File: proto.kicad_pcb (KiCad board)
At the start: 2 copper layers, 100 x 100 mm, 159 parts

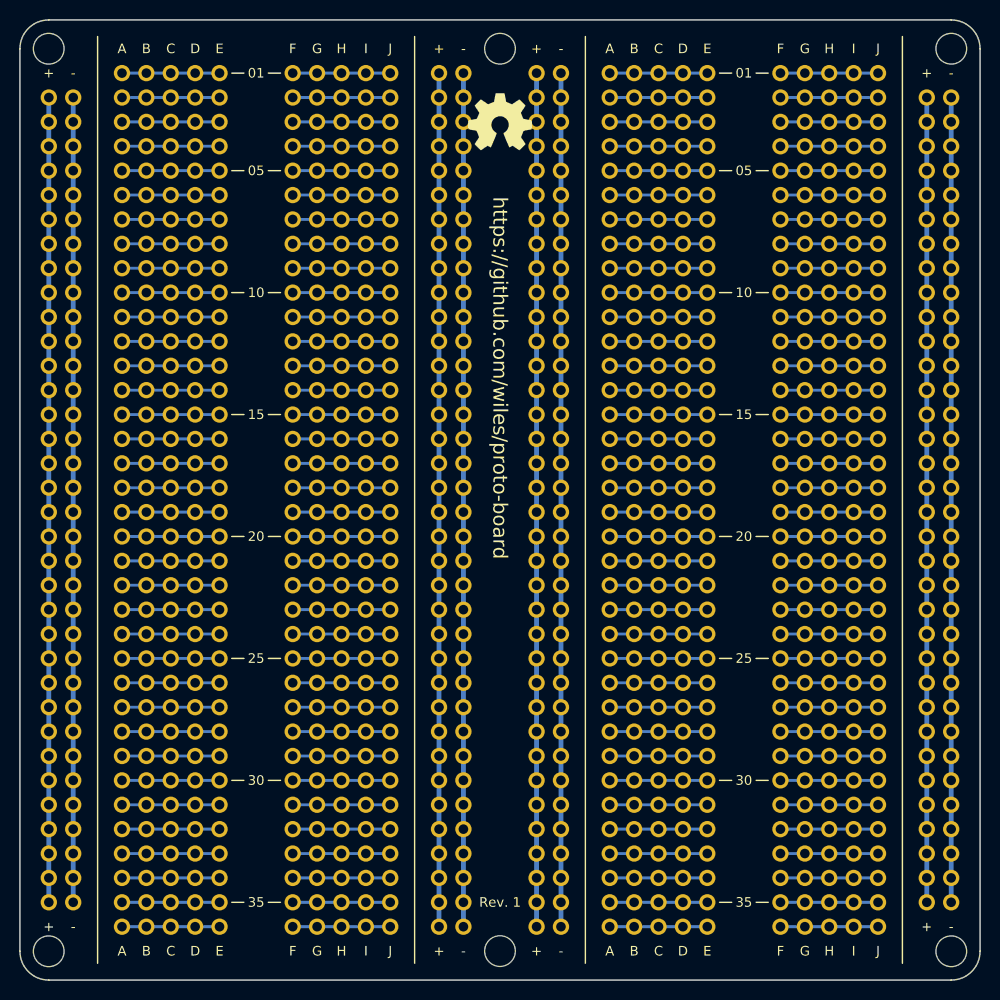
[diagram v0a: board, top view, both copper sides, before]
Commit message: increased trace width
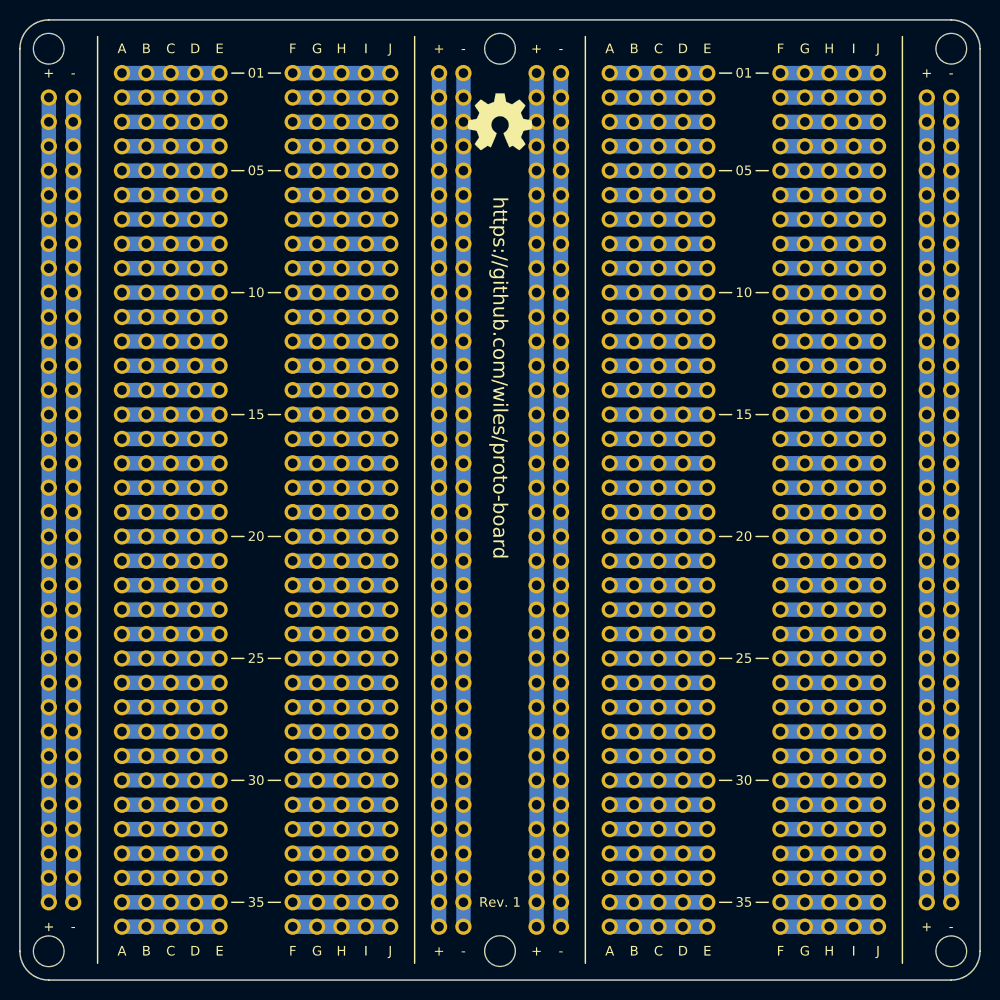
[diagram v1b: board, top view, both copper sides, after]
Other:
- net class Default removed
- net class VCC removed
